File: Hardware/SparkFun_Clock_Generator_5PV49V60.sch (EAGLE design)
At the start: 37 parts, among them J1 QWIIC_RIGHT_ANGLE, J2 QWIIC_RIGHT_ANGLE, U1 IDT_5P49V60_CLOCK_GENERATOR, Y1 16MHz

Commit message: Update ferrite bead
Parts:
- FB1: value FERRITE_BEAD -> FERRITE_BEAD-120_OHM-0402; device SparkFun-Coils:FERRITE_BEAD -> SparkFun-Coils:FERRITE_BEAD-120_OHM-0402
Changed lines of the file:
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@@
 <part name="C8" library="SparkFun-Capacitors" deviceset="1.0UF" device="-0402-16V-10%" value="1.0uF"/>
 <part name="C9" library="SparkFun-Capacitors" deviceset="10UF" device="-0603-6.3V-20%" value="10uF"/>
-<part name="FB1" library="SparkFun-Coils" deviceset="FERRITE_BEAD" device=""/>
+<part name="FB1" library="SparkFun-Coils" deviceset="FERRITE_BEAD-120_OHM" device="-0402" value="FERRITE_BEAD-120_OHM-0402"/>
 <part name="GND4" library="SparkFun-PowerSymbols" deviceset="GND" device=""/>
 <part name="SUPPLY4" library="SparkFun-PowerSymbols" deviceset="3.3V" device=""/>
@@
 </instance>
 <instance part="FB1" gate="G$1" x="27.94" y="139.7" smashed="yes" rot="R90">
-<attribute name="NAME" x="29.21" y="144.78" size="1.778" layer="95" font="vector" rot="R180"/>
+<attribute name="NAME" x="29.464" y="143.51" size="1.778" layer="95" font="vector" rot="R180"/>
 </instance>
 <instance part="GND4" gate="1" x="81.28" y="119.38" smashed="yes">

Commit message: Updates crystal footprint, and fixes routing
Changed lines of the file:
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@@
-</segment>
-<segment>
-<pinref part="Y1" gate="G$1" pin="GND"/>
-<pinref part="GND3" gate="1" pin="GND"/>
-<wire x1="55.88" y1="68.58" x2="55.88" y2="58.42" width="0.1524" layer="91"/>
-</segment>
-<segment>
-<pinref part="GND7" gate="1" pin="GND"/>
-<pinref part="C10" gate="G$1" pin="2"/>
-<wire x1="50.8" y1="58.42" x2="50.8" y2="63.5" width="0.1524" layer="91"/>
-</segment>
-<segment>
-<pinref part="C12" gate="G$1" pin="2"/>
-<pinref part="GND6" gate="1" pin="GND"/>
-<wire x1="60.96" y1="63.5" x2="60.96" y2="58.42" width="0.1524" layer="91"/>
 </segment>
 <segment>
@@
 <junction x="215.9" y="83.82"/>
 </segment>
+<segment>
+<pinref part="Y1" gate="G$1" pin="GND"/>
+<pinref part="GND3" gate="1" pin="GND"/>
+<wire x1="55.88" y1="68.58" x2="55.88" y2="58.42" width="0.1524" layer="91"/>
+</segment>
+<segment>
+<pinref part="C10" gate="G$1" pin="2"/>
+<pinref part="GND7" gate="1" pin="GND"/>
+<wire x1="50.8" y1="63.5" x2="50.8" y2="58.42" width="0.1524" layer="91"/>
+</segment>
+<segment>
+<pinref part="C12" gate="G$1" pin="2"/>
+<pinref part="GND6" gate="1" pin="GND"/>
+<wire x1="60.96" y1="63.5" x2="60.96" y2="58.42" width="0.1524" layer="91"/>
+</segment>
 </net>
 <net name="3.3V" class="0">
@@
 <net name="N$6" class="0">
 <segment>
+<wire x1="50.8" y1="71.12" x2="50.8" y2="73.66" width="0.1524" layer="91"/>
 <wire x1="50.8" y1="73.66" x2="50.8" y2="78.74" width="0.1524" layer="91"/>
 <wire x1="73.66" y1="78.74" x2="50.8" y2="78.74" width="0.1524" layer="91"/>
 <pinref part="U1" gate="G$1" pin="XIN"/>
+<pinref part="C10" gate="G$1" pin="1"/>
 <pinref part="Y1" gate="G$1" pin="2"/>
 <wire x1="53.34" y1="73.66" x2="50.8" y2="73.66" width="0.1524" layer="91"/>
-<pinref part="C10" gate="G$1" pin="1"/>
-<wire x1="50.8" y1="73.66" x2="50.8" y2="71.12" width="0.1524" layer="91"/>
 <junction x="50.8" y="73.66"/>
 </segment>
@@
 <pinref part="U1" gate="G$1" pin="XOUT"/>
 <wire x1="73.66" y1="73.66" x2="60.96" y2="73.66" width="0.1524" layer="91"/>
+<pinref part="C12" gate="G$1" pin="1"/>
+<wire x1="60.96" y1="71.12" x2="60.96" y2="73.66" width="0.1524" layer="91"/>
 <pinref part="Y1" gate="G$1" pin="1"/>
-<pinref part="C12" gate="G$1" pin="1"/>
-<wire x1="60.96" y1="73.66" x2="58.42" y2="73.66" width="0.1524" layer="91"/>
-<wire x1="60.96" y1="71.12" x2="60.96" y2="73.66" width="0.1524" layer="91"/>
+<wire x1="58.42" y1="73.66" x2="60.96" y2="73.66" width="0.1524" layer="91"/>
 <junction x="60.96" y="73.66"/>
 </segment>

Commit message: Radical change to design
* Moved all parts besides crystal and IC to "bottom of board"
  * This allows for better routing of Clock signals
* Adds 2.2Ohm series resistor to power rail
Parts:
- added R4: 2.2, SparkFun-Resistors:2.2OHM-0603-1/10W-5%
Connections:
- net 3.3V: now also R4.1, R4.2
- net OUT4: now also U1.OUT4B; no longer U1.OUT4
- net OUT4B: now also U1.OUT4; no longer U1.OUT4B
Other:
- note added: "v02"
- note removed: "v01"
- moved on the sheet: C7, C8

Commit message: Updates board with select jumper to enable select mode and fixes labels
* Also swaps clock out 4 and 4B
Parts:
- added JP2: JUMPER-SMT_2_NO_SILK, SparkFun-Jumpers:JUMPER-SMT_2_NO_SILK
- added R5: 10k, SparkFun-Resistors:10KOHM-0402-1/16W-1%
- LOGO1: value SFE_LOGO_NAME_FLAME.1_INCH -> SFE_LOGO_NAME.1_INCH; device SparkFun-Aesthetics:SFE_LOGO_NAME_FLAME.1_INCH -> SparkFun-Aesthetics:SFE_LOGO_NAME.1_INCH
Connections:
- new net N$7: JP2.1, R5.2
- new net SEL_I2CB: JP2.2, U1.SEL_I2CB
- net 3.3V: now also R5.1
- net OUT4: now also J3.1, U1.OUT4; no longer J3.2, U1.OUT4B
- net OUT4B: now also J3.2, U1.OUT4B; no longer J3.1, U1.OUT4
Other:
- note added: "Default Unshifted 7 bit Address: 0x6A Alternate Address: 0x6B"
- note added: "Fill jumper to enable Selection Mode."
- note removed: "Default Unshifted 7 bit Address: 0xD4"
- moved on the sheet: D1, JP1, LED, R1, R2, R3

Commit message: Improves ground plane pour, adds some more vias, updates packages of clock and crystal
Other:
- note added: "Selection Mode: Changes behavior of 12C lines to "selection" lines which determines which RAM settings to load on power up. See pg. 15 of Datasheet."
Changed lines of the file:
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@@
 <part name="FD4" library="SparkFun-Aesthetics" deviceset="FIDUCIAL" device="UFIDUCIAL"/>
 <part name="GND3" library="SparkFun-PowerSymbols" deviceset="GND" device=""/>
-<part name="JP1" library="SparkFun-Jumpers" deviceset="JUMPER-SMT_3_2-NC_TRACE" device="_SILK"/>
+<part name="JP1" library="SparkFun-Jumpers" deviceset="JUMPER-SMT_3_2-NC_TRACE" device="_SILK" package3d_urn="urn:adsk.eagle:package:39289/1"/>
 <part name="R1" library="SparkFun-Resistors" deviceset="10KOHM" device="-0402-1/16W-1%" value="10k"/>
 <part name="R2" library="SparkFun-Resistors" deviceset="10KOHM" device="-0402-1/16W-1%" value="10k"/>
@@
 <part name="R3" library="SparkFun-Resistors" deviceset="1KOHM" device="-0402-1/16W-1%"/>
 <part name="GND8" library="SparkFun-PowerSymbols" deviceset="GND" device=""/>
-<part name="LED" library="SparkFun-Jumpers" deviceset="JUMPER-SMT_2_NC_TRACE" device="_SILK"/>
+<part name="LED" library="SparkFun-Jumpers" deviceset="JUMPER-SMT_2_NC_TRACE" device="_SILK" package3d_urn="urn:adsk.eagle:package:39281/1"/>
 <part name="SUPPLY6" library="SparkFun-PowerSymbols" deviceset="3.3V" device=""/>
 <part name="LOGO1" library="SparkFun-Aesthetics" deviceset="SFE_LOGO_NAME" device=".1_INCH" value="SFE_LOGO_NAME.1_INCH"/>
@@
 <text x="190.5" y="165.1" size="1.27" layer="97" font="vector">Fill jumper to enable
 Selection Mode.</text>
+<text x="215.9" y="172.72" size="1.27" layer="97" font="vector">Selection Mode:
+Changes behavior of 12C lines to
+"selection" lines which determines
+which RAM settings to load
+on power up. See pg. 15 of Datasheet.
+</text>
+<wire x1="198.12" y1="177.8" x2="198.12" y2="180.34" width="0.2032" layer="97" style="dashdot"/>
+<wire x1="198.12" y1="180.34" x2="213.36" y2="180.34" width="0.2032" layer="97" style="dashdot"/>
 </plain>
 <instances>
@@
 <segment>
 <pinref part="U1" gate="G$1" pin="SEL_I2CB"/>
-<wire x1="73.66" y1="68.58" x2="71.12" y2="68.58" width="0.1524" layer="91"/>
-<label x="71.12" y="68.58" size="1.27" layer="95" rot="R180" xref="yes"/>
-</segment>
-<segment>
+<wire x1="109.22" y1="68.58" x2="111.76" y2="68.58" width="0.1524" layer="91"/>
+<label x="111.76" y="68.58" size="1.27" layer="95" xref="yes"/>
+</segment>
+<segment>

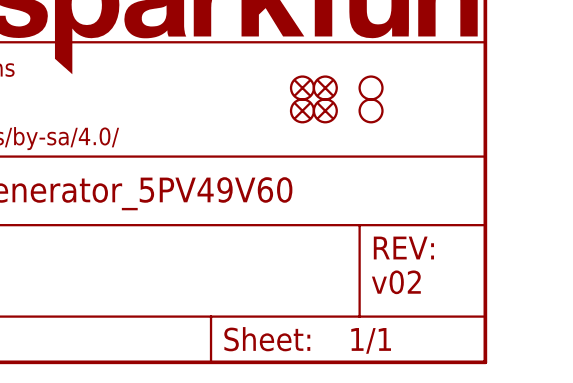
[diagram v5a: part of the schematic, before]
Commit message: Fixes "SEL" text, adds second ground pour for clock lines isolate only, fixes power shorting through ferrite and resistor
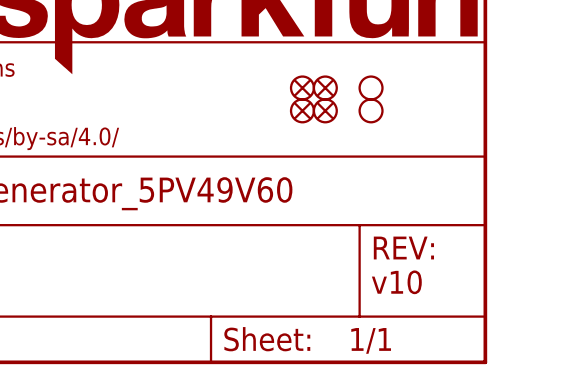
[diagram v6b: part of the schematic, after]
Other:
- note added: "v10"
- note removed: "v02"
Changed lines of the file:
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@@
 <plain>
 <text x="166.37" y="11.684" size="2.54" layer="94" font="vector">Elias Santistevan</text>
-<text x="236.22" y="7.62" size="2.54" layer="94" font="vector">v02</text>
+<text x="236.22" y="7.62" size="2.54" layer="94" font="vector">v10</text>
 <wire x1="68.58" y1="99.06" x2="60.96" y2="99.06" width="0.2032" layer="97" style="dashdot"/>
 <wire x1="60.96" y1="99.06" x2="60.96" y2="114.3" width="0.2032" layer="97" style="dashdot"/>

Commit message: Fixes air wires, adds clock generator to eagle library, removes buzzard label folder
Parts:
- U1: device clock:IDT_5P49V60_CLOCK_GENERATOR -> SparkFun-IC-Special-Function:IDT_5P49V60_CLOCK_GENERATOR
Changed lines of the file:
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@@
 <part name="J1" library="SparkFun-Connectors" deviceset="QWIIC_CONNECTOR" device="JS-1MM" value="QWIIC_RIGHT_ANGLE"/>
 <part name="J2" library="SparkFun-Connectors" deviceset="QWIIC_CONNECTOR" device="JS-1MM" value="QWIIC_RIGHT_ANGLE"/>
-<part name="U1" library="clock" deviceset="IDT_5P49V60_CLOCK_GENERATOR" device=""/>
+<part name="U1" library="SparkFun-IC-Special-Function" deviceset="IDT_5P49V60_CLOCK_GENERATOR" device=""/>
 <part name="GND1" library="SparkFun-PowerSymbols" deviceset="GND" device=""/>
 <part name="SUPPLY1" library="SparkFun-PowerSymbols" deviceset="3.3V" device=""/>

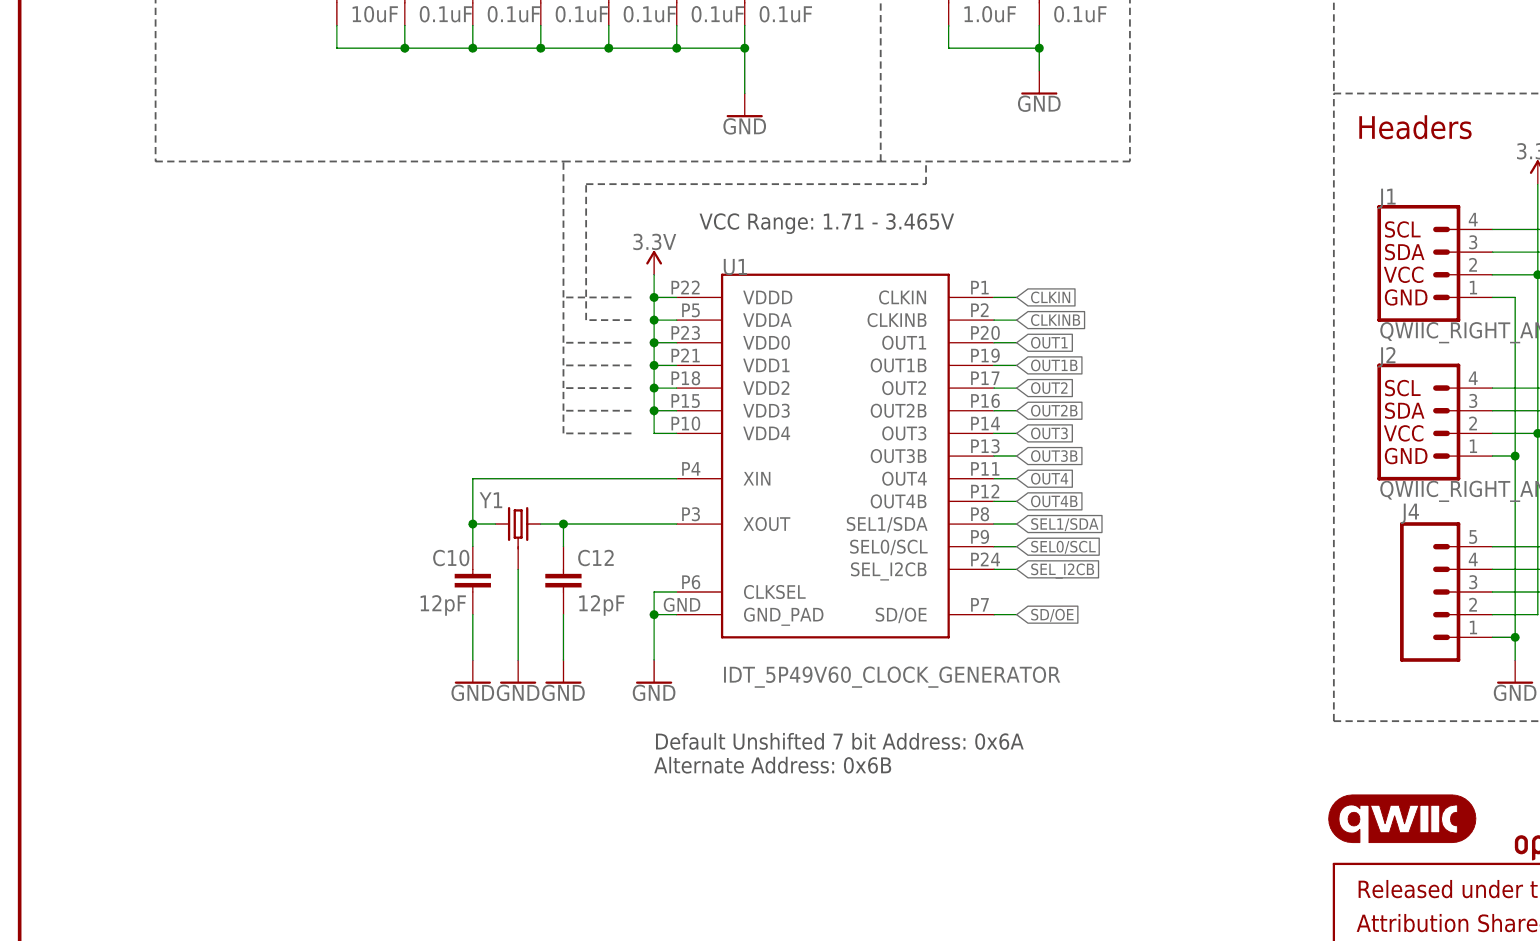
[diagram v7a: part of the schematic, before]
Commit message: Adds more info to schematic, removes old production files and unnecessary README's
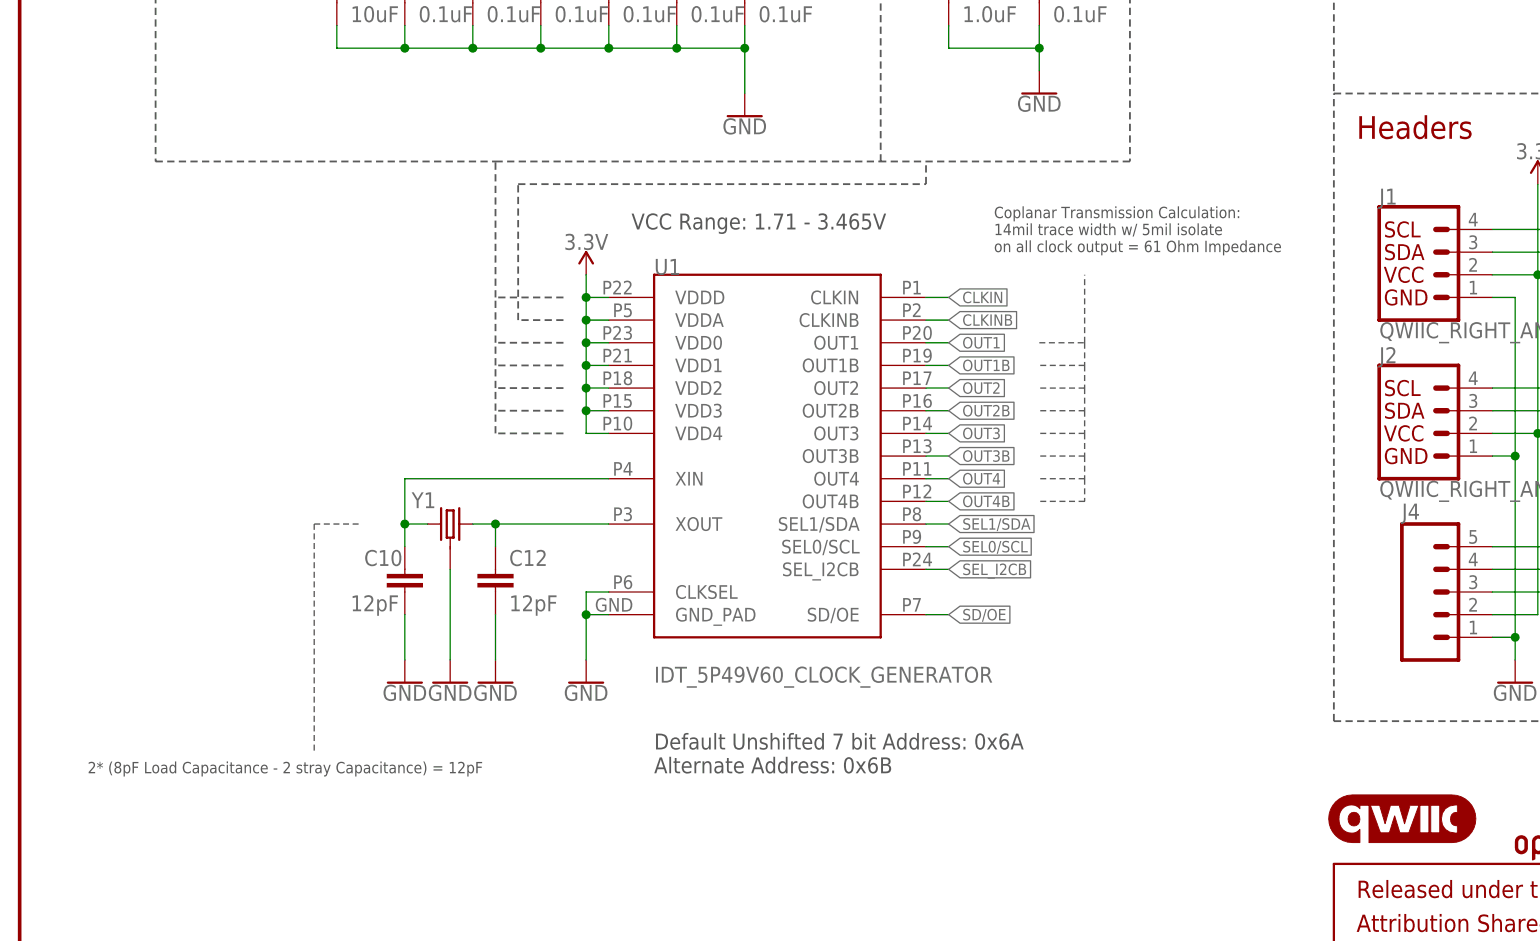
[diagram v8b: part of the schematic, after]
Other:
- note added: "2* (8pF Load Capacitance - 2 stray Capacitance) = 12pF"
- note added: "Coplanar Transmission Calculation: 14mil trace width w/ 5mil isolate on all clock output = 61 Ohm Impedance"
- moved on the sheet: C10, C12, U1, Y1
